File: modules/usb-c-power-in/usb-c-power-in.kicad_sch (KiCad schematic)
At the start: 1 part, among them J1 Conn_01x02

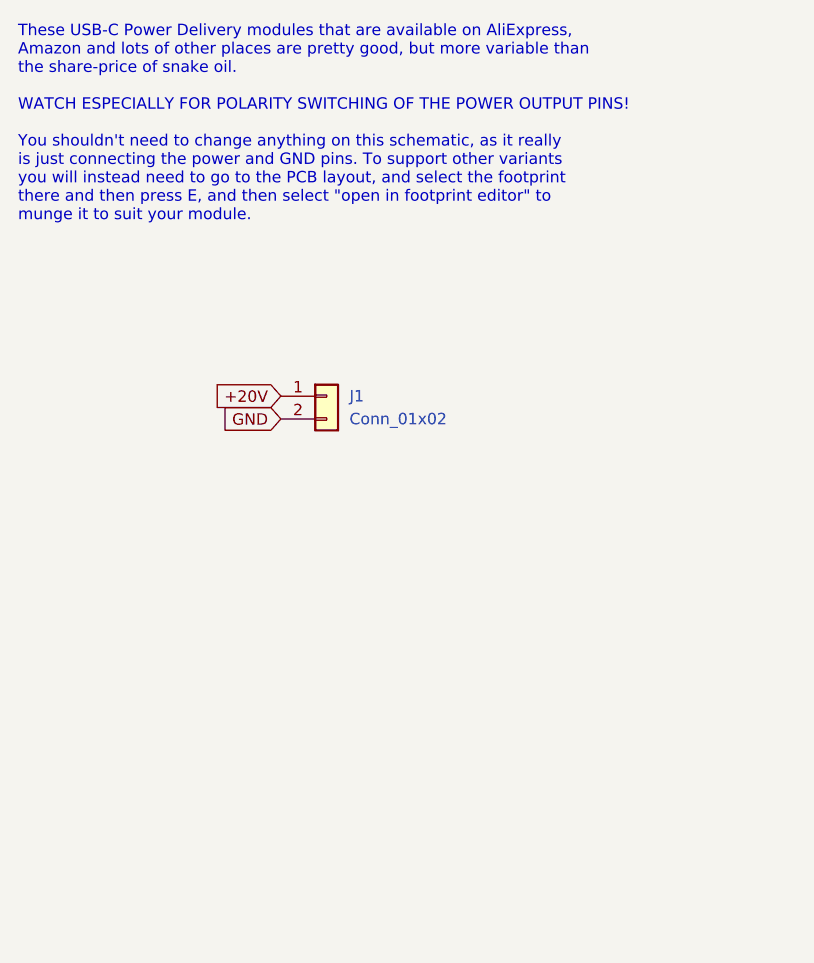
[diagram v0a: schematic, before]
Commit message: finish usb-c power in module and generate gerbers
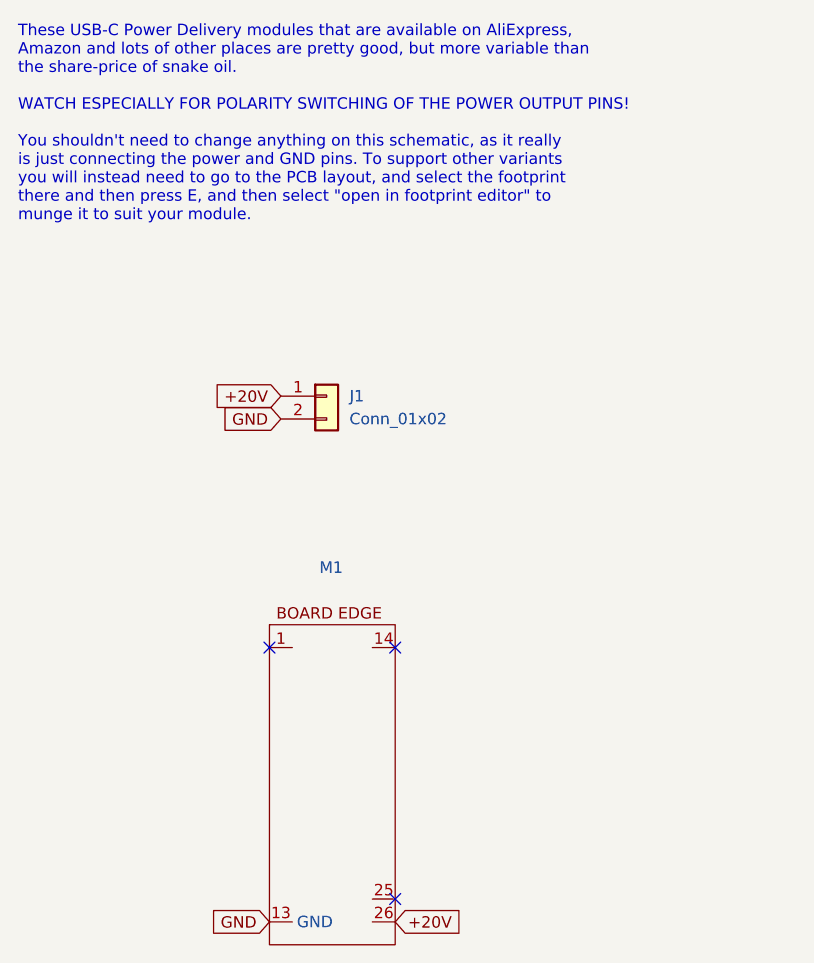
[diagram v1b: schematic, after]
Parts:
- added M1: ~, MegaCastle:MegaCastle2x13-Module-I14.0x28.2-M800C00C-PANEL-NIBBLE, symbol MegaCastle:MegaCastle2x13-Module-I14.0x28.2-M800C00C-NOCUTOUT-EDGE
- J1: footprint (none) -> Connector_PinHeader_2.54mm:PinHeader_1x02_P2.54mm_Vertical
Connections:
- net +20V: now also M1.26
- net GND: now also M1.13 (GND)
- no-connect marks 0 -> 3
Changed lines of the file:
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@@
 	(generator_version "8.0")
 	(paper "A4")
+	(no_connect
+		(at 71.12 120.65)
+	)
+	(no_connect
+		(at 57.15 92.71)
+	)
+	(no_connect
+		(at 71.12 92.71)
+	)
 	(text "These USB-C Power Delivery modules that are available on AliExpress, \nAmazon and lots of other places are pretty good, but more variable than\nthe share-price of snake oil.\n\nWATCH ESPECIALLY FOR POLARITY SWITCHING OF THE POWER OUTPUT PINS!\n\nYou shouldn't need to change anything on this schematic, as it really\nis just connecting the power and GND pins. To support other variants\nyou will instead need to go to the PCB layout, and select the footprint\nthere and then press E, and then select \"open in footprint editor\" to\nmunge it to suit your module."
 		(exclude_from_sim no)
@@
 		)
 	)
+	(global_label "GND"
+		(shape input)
+		(at 57.15 123.19 180)
+		(fields_autoplaced yes)
+		(effects
+			(font
+				(size 1.27 1.27)
+			)
+			(justify right)
+		)
+		(property "Intersheetrefs" "${INTERSHEET_REFS}"
+			(at 50.2943 123.19 0)
+			(effects
+				(font
+					(size 1.27 1.27)
+				)
+				(justify right)
+				(hide yes)
+			)
+		)
+	)
 	(global_label "+20V"
 		(shape input)
@@
 				(justify right)
 				(hide yes)
+			)
+		)
+	)
+	(global_label "+20V"
+		(shape input)
+		(at 71.12 123.19 0)
+		(fields_autoplaced yes)
+		(effects
+			(font
+				(size 1.27 1.27)
+			)
+			(justify left)
+		)
+		(property "Intersheetrefs" "${INTERSHEET_REFS}"
+			(at 79.1852 123.19 0)
+			(effects
+				(font
+					(size 1.27 1.27)
+				)
+				(justify left)
+				(hide yes)
+			)
+		)
+	)
+	(symbol
+		(lib_id "MegaCastle:MegaCastle2x13-Module-I14.0x28.2-M800C00C-NOCUTOUT-EDGE")
+		(at 63.5 107.95 0)
+		(unit 1)
+		(exclude_from_sim no)
+		(in_bom yes)
+		(on_board yes)
+		(dnp no)
+		(fields_autoplaced yes)
+		(property "Reference" "M1"
+			(at 64.0038 83.82 0)
+			(effects
+				(font
+					(size 1.27 1.27)
+				)
+			)
+		)
+		(property "Value" "~"
+			(at 64.0038 86.36 0)
+			(effects
+				(font
+					(size 1.27 1.27)
+				)
+			)
+		)
+		(property "Footprint" "MegaCastle:MegaCastle2x13-Module-I14.0x28.2-M800C00C-PANEL-NIBBLE"
+			(at 63.5 130.81 0)
+			(effects
+				(font
+					(size 1.27 1.27)
+				)
+				(hide yes)
+			)
+		)
+		(property "Datasheet" ""
+			(at 63.5 102.87 0)
+			(effects
+				(font
+					(size 1.27 1.27)
+				)
+				(hide yes)
+			)
+		)
+		(property "Description" "Generated using footprint-gen .. 14 28 5 M800C00C"
+			(at 63.5 107.95 0)
+			(effects
+				(font
+					(size 1.27 1.27)
+				)
+				(hide yes)
+			)
+		)
+		(pin "26"
+		)
+		(pin "25"
+		)
+		(pin "14"
+		)
+		(pin "13"
+		)
+		(pin "1"
+		)
+		(instances
+			(project ""
+				(path "/1ab374f1-1696-497e-a408-710496bc66f3"
+					(reference "M1")
+					(unit 1)
+				)
 			)
 		)
@@
 			)
 		)
-		(property "Footprint" ""
+		(property "Footprint" "Connector_PinHeader_2.54mm:PinHeader_1x02_P2.54mm_Vertical"
 			(at 63.5 64.77 0)
 			(effects
